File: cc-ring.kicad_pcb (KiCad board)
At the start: 2 copper layers, 75 x 5.5 mm, 39 parts, among them J1 Battery, J2 Charge/debug, J3 Battery, U1 STM32L431CCYx, U2 BQ297xy, U3 CSD83325L

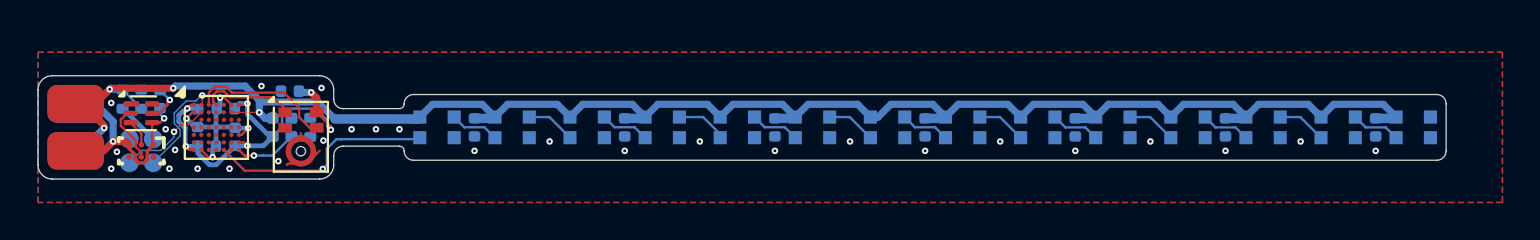
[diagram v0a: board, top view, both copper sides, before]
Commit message: magnetic charge connector
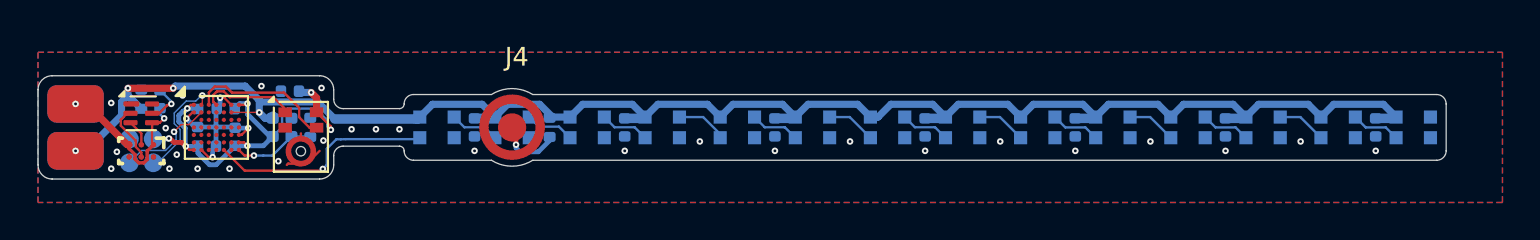
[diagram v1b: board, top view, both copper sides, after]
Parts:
- added J4: Charge, SolderPads:MageneticChargeConnector, F.Cu at (190.2, 71.0)
- J2: value Charge/debug -> Debug
- R2: value 220 -> 120
- moved R2 22.8 mm to (192.2, 71.0)
- turned J1 to 180 degrees
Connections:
- J2 pad 1: Net-(J2-Pin_1) -> VDD
- R2 pad 2: Net-(J2-Pin_1) -> Net-(J4-Pin_1)
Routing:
- net +BATT: track 96.1 -> 92.5 mm
- net Net-(J4-Pin_1): track 0.00 -> 3.50 mm, vias 0 -> 1
- net -BATT: track 11.8 -> 9.41 mm
- net Net-(J2-Pin_1): track 2.30 -> 0.00 mm
- net VDD: track 21.9 -> 23.8 mm, vias 6 -> 7
- net GND: vias 33 -> 32
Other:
- outline, holes or cut-outs redrawn

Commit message: update layout for magentic charge
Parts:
- D10: footprint Diode_SMD:D_0402_1005Metric -> Diode_SMD:D_SOD-523
- moved D10 0.20 mm to (177.3, 71.0)
